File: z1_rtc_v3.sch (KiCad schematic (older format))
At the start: 61 parts, among them J1 Conn_01x05, J10 Conn_01x02, J2 61200621621, J3 Conn_01x11, J4 Conn_01x11, J5 Conn_01x11, J6 Conn_01x11, J7 691137710002, J8 USB_B_Micro, J9 Conn_01x02, U1 LCMXO2-1200HC-4SG32C, U2 ATmega328PB-AU, U3 FT230XS, Y1 Crystal_Small

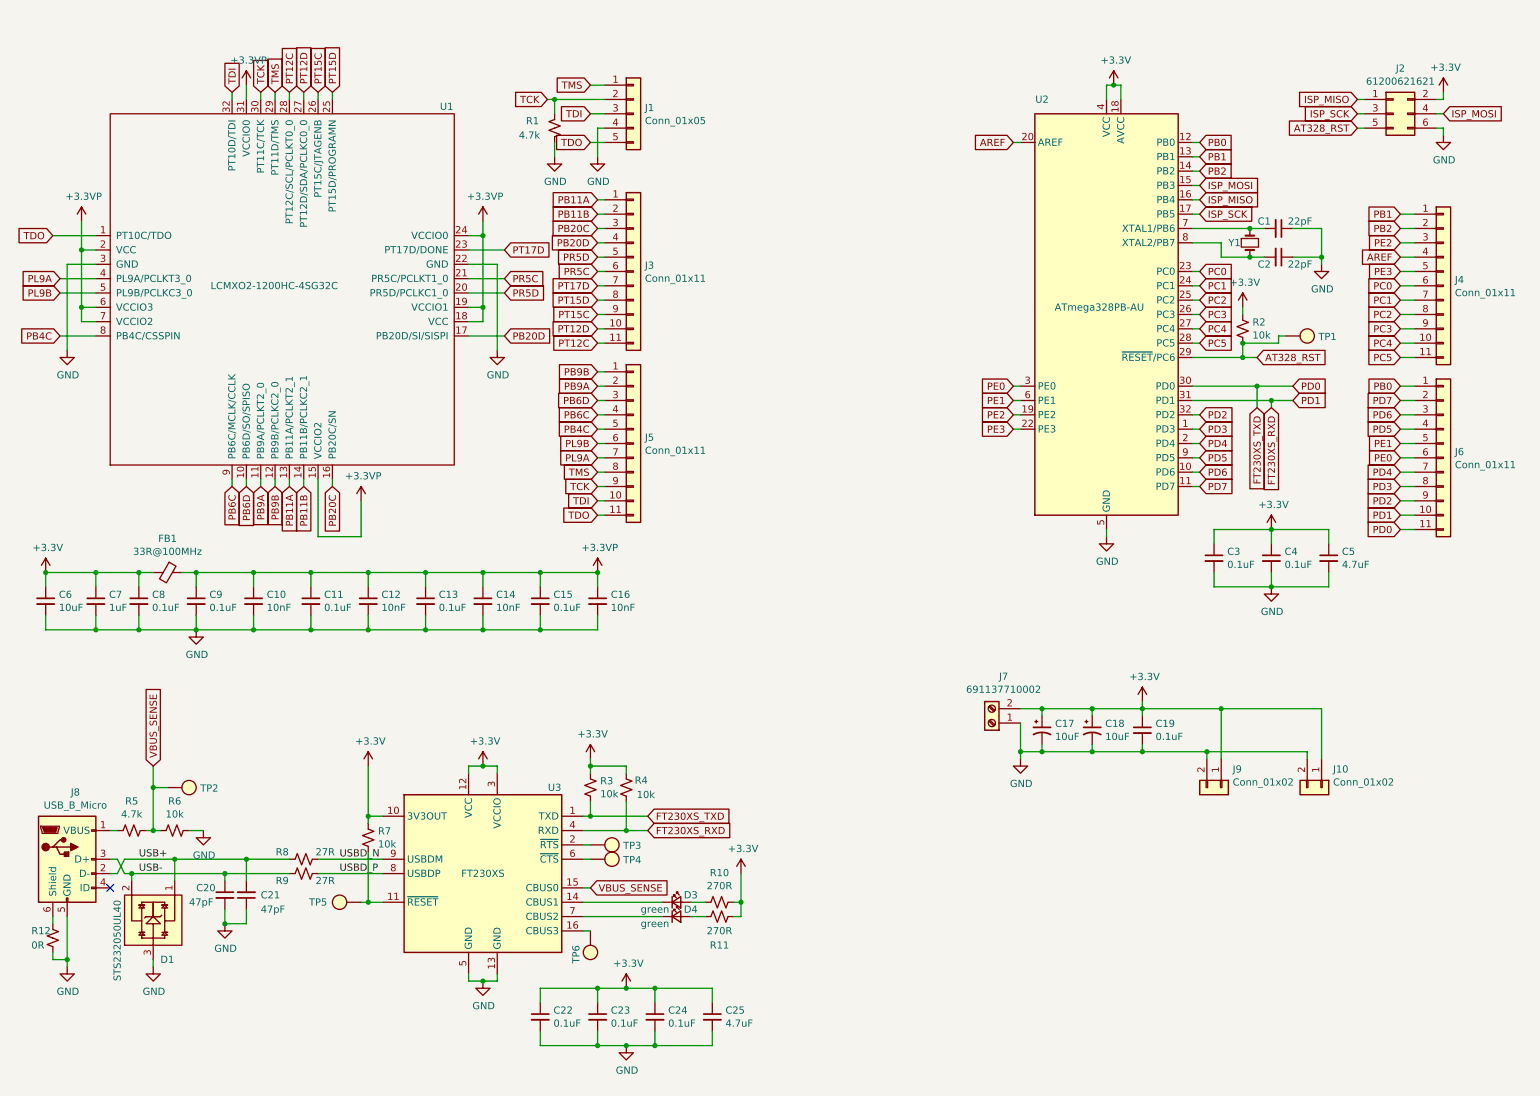
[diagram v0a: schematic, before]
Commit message: finished routing v3.3
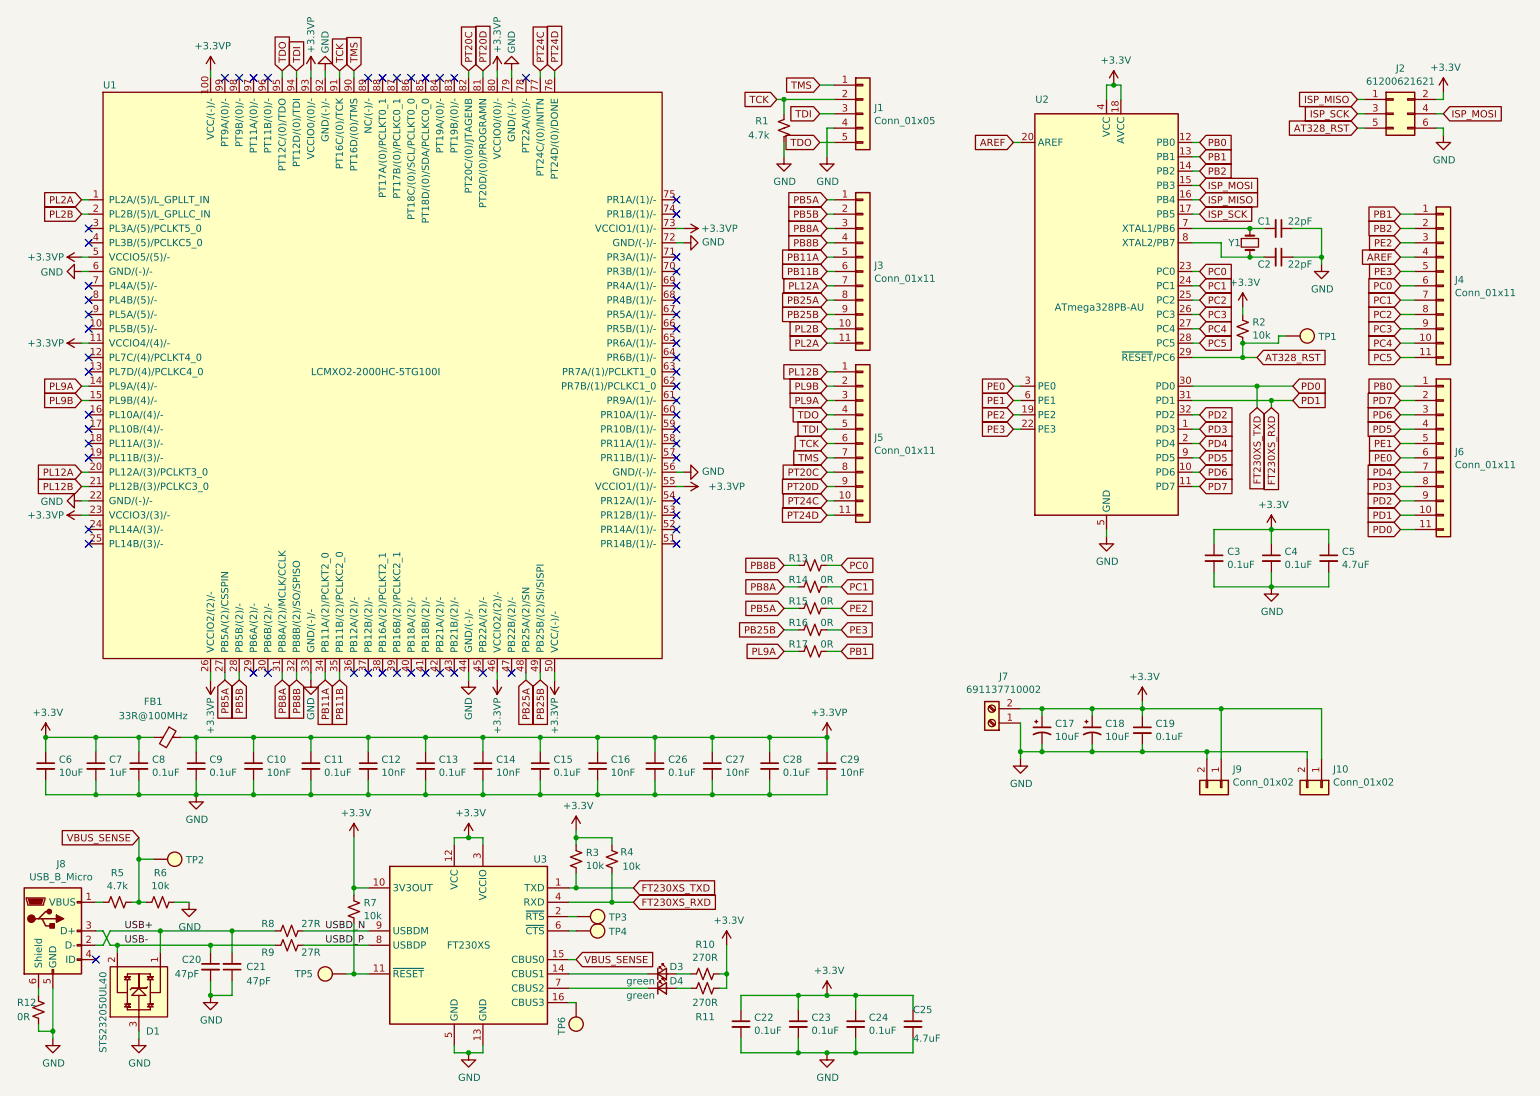
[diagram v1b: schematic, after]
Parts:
- removed U1: LCMXO2-1200HC-4SG32C, Package_DFN_QFN:QFN-32-1EP_5x5mm_P0.5mm_EP3.1x3.1mm, symbol z1_rtc_v3:LCMXO2-1200HC-4SG32C
- added C26, C28: 0.1uF, Capacitor_SMD:C_0603_1608Metric, symbol Device:C_Small
- added C27, C29: 10nF, Capacitor_SMD:C_0805_2012Metric, symbol Device:C_Small
- added R13, R14, R15, R16, R17: 0R, Resistor_SMD:R_0603_1608Metric, symbol Device:R_Small_US
- added U1: LCMXO2-2000HC-5TG100I, Package_QFP:TQFP-100_14x14mm_P0.5mm, symbol z1_rtc_v3:LCMXO2-2000HC-5TG100I
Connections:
- net PB4C is gone; now on net TDI: J5.5 (Pin_5)
- net PB6C is gone; now on net TDO: J5.4 (Pin_4)
- net PB6D is gone; now on net PL9A: J5.3 (Pin_3)
- net PB9A is gone; now on net PL9B: J5.2 (Pin_2)
- net PR5C is gone; now on net PB11B: J3.6 (Pin_6)
- net PR5D is gone; now on net PB11A: J3.5 (Pin_5)
- net +3.3VP: now also C26.1, C27.1, C28.1, C29.1, U1.100 (VCC/(-)/-), U1.11 (VCCIO4/(4)/-), U1.23 (VCCIO3/(3)/-), U1.26 (VCCIO2/(2)/-), U1.46 (VCCIO2/(2)/-), U1.5 (VCCIO5/(5)/-), U1.50 (VCC/(-)/-), U1.55 (VCCIO1/(1)/-), U1.73 (VCCIO1/(1)/-), U1.80 (VCCIO0/(0)/-), U1.93 (VCCIO0/(0)/-)
- net GND: now also C26.2, C27.2, C28.2, C29.2, U1.22 (GND/(-)/-), U1.33 (GND/(-)/-), U1.44 (GND/(-)/-), U1.56 (GND/(-)/-), U1.6 (GND/(-)/-), U1.72 (GND/(-)/-), U1.79 (GND/(-)/-), U1.92 (GND/(-)/-)
- net PB1: now also R17.1
- net PB11A: now also U1.34 (PB11A/(2)/PCLKT2_0); no longer J3.1 (Pin_1)
- net PB11B: now also U1.35 (PB11B/(2)/PCLKC2_0); no longer J3.2 (Pin_2)
- net PC0: now also R13.1
- net PC1: now also R14.1
- net PE2: now also R15.1
- net PE3: now also R16.1
- net PL9A: now also R17.2, U1.14 (PL9A/(4)/-); no longer J5.7 (Pin_7)
- net PL9B: now also U1.15 (PL9B/(4)/-); no longer J5.6 (Pin_6)
- net TCK: now also J5.6 (Pin_6), U1.91 (PT16C/(0)/TCK); no longer J5.9 (Pin_9)
- net TDI: now also U1.94 (PT12D/(0)/TDI); no longer J5.10 (Pin_10)
- net TDO: now also U1.95 (PT12C/(0)/TDO); no longer J5.11 (Pin_11)
- net TMS: now also J5.7 (Pin_7), U1.90 (PT16D/(0)/TMS); no longer J5.8 (Pin_8)
- net PB20C renamed PB8A
- net PB8A: now also R14.2, U1.31 (PB8A/(2)/MCLK/CCLK)
- net PB20D renamed PB8B
- net PB8B: now also R13.2, U1.32 (PB8B/(2)/SO/SPISO)
- net PB9B renamed PL12B
- net PL12B: now also U1.21 (PL12B/(3)/PCLKC3_0)
- net PT12C renamed PL2A
- net PL2A: now also U1.1 (PL2A/(5)/L_GPLLT_IN)
- net PT12D renamed PL2B
- net PL2B: now also U1.2 (PL2B/(5)/L_GPLLC_IN)
- net PT15C renamed PB25B
- net PB25B: now also R16.2, U1.49 (PB25B/(2)/SI/SISPI)
- net PT15D renamed PB25A
- net PB25A: now also U1.48 (PB25A/(2)/SN)
- net PT17D renamed PL12A
- net PL12A: now also U1.20 (PL12A/(3)/PCLKT3_0)
- new net PB5A: J3.1 (Pin_1), R15.2, U1.27 (PB5A/(2)/CSSPIN)
- new net PB5B: J3.2 (Pin_2), U1.28 (PB5B/(2)/-)
- new net PT20C: J5.8 (Pin_8), U1.82 (PT20C/(0)/JTAGENB)
- new net PT20D: J5.9 (Pin_9), U1.81 (PT20D/(0)/PROGRAMN)
- new net PT24C: J5.10 (Pin_10), U1.77 (PT24C/(0)/INITN)
- new net PT24D: J5.11 (Pin_11), U1.76 (PT24D/(0)/DONE)
- no-connect marks 1 -> 60
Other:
- moved on the sheet: C10, C11, C12, C13, C14, C15, C16, C20, C21, C22, C23, C24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
